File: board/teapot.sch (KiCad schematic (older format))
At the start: 48 parts, among them J1 MICROUSB, P1 BATT, P2 SMA, P3 SWD_TC, Q1 TEPT4400, U1 TPS79333DBVR, U2 TLV61225, U4 RFM69W, U5 STM32L052K6T6, U6 HTU21D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

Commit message: Sch: removed usb, pwr led, swd
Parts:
- removed C2: 100n, Capacitors_SMD:C_0603, symbol C
- removed C4: 10n, Capacitors_SMD:C_0603, symbol C
- removed C5: 10u, Capacitors_SMD:C_0603, symbol C
- removed D2: RED, LEDs:LED_0805, symbol LED
- removed J1: MICROUSB, agg:MICROUSB_MOLEX_47589-0001, symbol MICROUSB
- removed R2: 1k, Resistors_SMD:R_0603, symbol R
- removed U1: TPS79333DBVR, TO_SOT_Packages_SMD:SOT-23-5, symbol TPS79333DBVR
- removed U8: SWD, footprints:SWD, symbol SWD
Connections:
- net labels removed: +5V
- wire segments 91 -> 78
- no-connect marks 14 -> 10
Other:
- note removed: "10nF cap optional\nfor noise reduction"
- note removed: "USB"
- moved on the sheet: C1, C3, D1, D4, D5, L1, P1, R1, R5, R6, TP2, TP3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

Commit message: Migated PSU and boilerplate to new QFN-64 micro
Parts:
- removed U5: STM32L052K6T6, footprints:LQFP32_ST, symbol STM32L052K6T6
- added C?: 100n, Capacitors_SMD:C_0603, symbol C
- added IC?: STM32F0xxCxUx, agg:QFN-48-EP-ST, symbol STM32F0xxCxUx
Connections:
- net labels removed: USB_D+, USB_D-
- wire segments 78 -> 74
- no-connect marks 10 -> 5
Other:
- note added: "VBAT"
- note added: "VDD"
- note added: "VDDA"
- moved on the sheet: C10, C11, C12, C13, C15, C16, C8, C9, R3, R4, TP4, TP5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

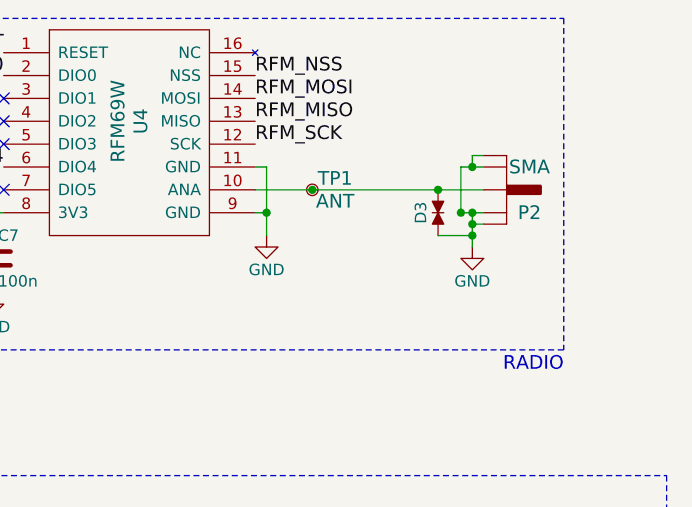
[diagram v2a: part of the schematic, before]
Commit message: Ripped up old PCB.
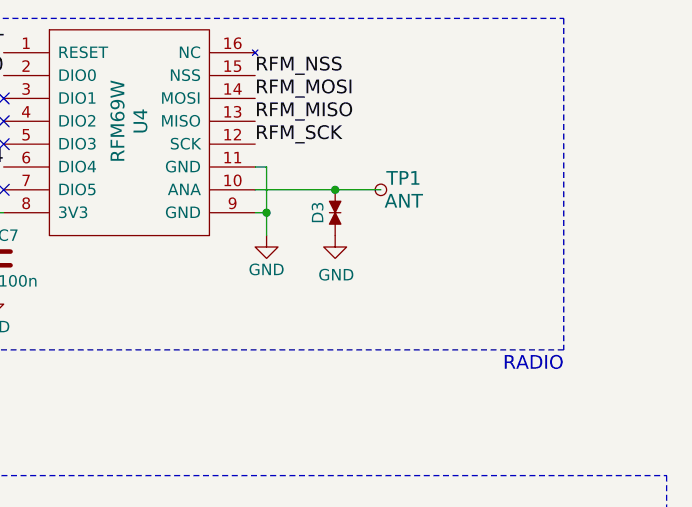
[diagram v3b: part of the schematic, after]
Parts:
- removed P2: SMA, footprints:SMA-142-0701-801, symbol SMA
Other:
- moved on the sheet: D3, TP1
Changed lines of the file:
@@
 RFM_SCK
-$Comp
-L SMA P2
-U 1 1 5670BE45
-P 10050 1650
-F 0 "P2" H 10150 1550 60  0000 C CNN
-F 1 "SMA" H 10150 1750 60  0000 C CNN
-F 2 "footprints:SMA-142-0701-801" H 10050 1650 60  0001 C CNN
-F 3 "" H 10050 1650 60  0000 C CNN
-F 4 "1342651" H 10050 1650 60  0001 C CNN "Farnell"
-	1    10050 1650
-	1    0    0    -1
-$EndComp
 $Comp
 L TestPoint TP1
 U 1 1 5670C17A
-P 9200 1650
-F 0 "TP1" H 9300 1700 60  0000 C CNN
-F 1 "ANT" H 9300 1600 60  0000 C CNN
-F 2 "footprints:Test_point" H 9200 1650 60  0001 C CNN
-F 3 "" H 9200 1650 60  0000 C CNN
-	1    9200 1650
-	1    0    0    -1
-$EndComp
-$Comp
-L GND #PWR014
-U 1 1 5670C5C3
-P 9900 1900
-F 0 "#PWR014" H 9900 1650 50  0001 C CNN
-F 1 "GND" H 9900 1750 50  0000 C CNN
-F 2 "" H 9900 1900 50  0000 C CNN
-F 3 "" H 9900 1900 50  0000 C CNN
-	1    9900 1900
+P 9500 1650
+F 0 "TP1" H 9600 1700 60  0000 C CNN
+F 1 "ANT" H 9600 1600 60  0000 C CNN
+F 2 "footprints:Test_point" H 9500 1650 60  0001 C CNN
+F 3 "" H 9500 1650 60  0000 C CNN
+	1    9500 1650
 	1    0    0    -1
 $EndComp
@@
 L TVS_small D3
 U 1 1 56787864
-P 9750 1750
-F 0 "D3" H 9750 1825 50  0000 C CNN
-F 1 "TVS_small" H 9750 1675 50  0001 C CNN
-F 2 "Resistors_SMD:R_0603" H 9750 1750 60  0001 C CNN
-F 3 "http://www.farnell.com/datasheets/1772768.pdf" H 9750 1750 60  0001 C CNN
-F 4 "2368174" H 9750 1750 60  0001 C CNN "Farnell"
-	1    9750 1750
+P 9300 1750
+F 0 "D3" H 9300 1825 50  0000 C CNN
+F 1 "TVS_small" H 9300 1675 50  0001 C CNN
+F 2 "Resistors_SMD:R_0603" H 9300 1750 60  0001 C CNN
+F 3 "http://www.farnell.com/datasheets/1772768.pdf" H 9300 1750 60  0001 C CNN
+F 4 "2368174" H 9300 1750 60  0001 C CNN "Farnell"
+	1    9300 1750
 	0    -1   -1   0
 $EndComp
@@
 Connection ~ 9850 4050
 Wire Wire Line
-	8950 1650 9950 1650
-Wire Wire Line
-	9850 1550 9950 1550
-Wire Wire Line
-	9900 1550 9900 1500
-Wire Wire Line
-	9900 1500 9950 1500
-Connection ~ 9900 1550
-Wire Wire Line
-	9900 1750 9900 1900
-Wire Wire Line
-	9900 1800 9950 1800
-Connection ~ 9900 1750
-Connection ~ 9200 1650
-Wire Wire Line
-	9850 1550 9850 1750
-Connection ~ 9850 1750
-Connection ~ 9900 1800
-Wire Wire Line
-	9850 1750 9950 1750
-Wire Wire Line
 	8950 1550 9000 1550
 Wire Wire Line
@@
 Wire Wire Line
 	7500 3250 7550 3250
-Connection ~ 9750 1650
+Connection ~ 9300 1650
 Wire Wire Line
 	1900 1050 1900 1500
@@
 Wire Wire Line
 	2200 1650 2200 1850
-Wire Wire Line
-	9750 1850 9900 1850
-Connection ~ 9900 1850
 Wire Wire Line
 	1900 1050 2050 1050
@@
 Text Notes -4050 2800 0    60   ~ 0
 VBAT
+$Comp
+L GND #PWR?
+U 1 1 5764CF24
+P 9300 1850
+F 0 "#PWR?" H 9300 1600 50  0001 C CNN
+F 1 "GND" H 9305 1677 50  0000 C CNN
+F 2 "" H 9300 1850 50  0000 C CNN
+F 3 "" H 9300 1850 50  0000 C CNN
+	1    9300 1850
+	1    0    0    -1
+$EndComp
+Wire Wire Line
+	8950 1650 9500 1650
 $EndSCHEMATC

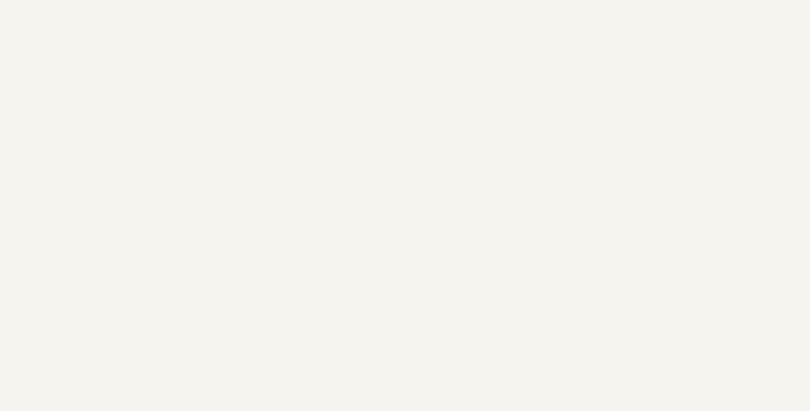
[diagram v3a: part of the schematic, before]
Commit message: Added AMG88 part/fp
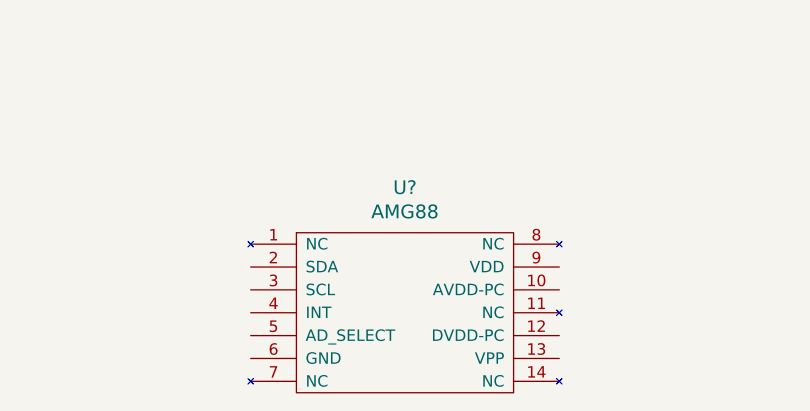
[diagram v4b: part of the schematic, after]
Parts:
- added U?: AMG88, footprints:AMG88, symbol AMG88
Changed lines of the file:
@@
 LIBS:tept
 LIBS:rfm69w
-LIBS:sma
 LIBS:testpoint
-LIBS:swd
-LIBS:tps79333dbvr
 LIBS:tvs_small
 LIBS:microusb
 LIBS:swd_tc
 LIBS:stm32f0xxcxux
+LIBS:amg88
 LIBS:teapot-cache
 EELAYER 25 0
@@
 Wire Wire Line
 	8950 1650 9500 1650
+$Comp
+L AMG88 U?
+U 1 1 57642B50
+P -3100 7400
+F 0 "U?" H -3125 7947 60  0000 C CNN
+F 1 "AMG88" H -3125 7841 60  0000 C CNN
+F 2 "footprints:AMG88" H -3150 7800 60  0001 C CNN
+F 3 "http://www.farnell.com/datasheets/1995912.pdf" H -3150 7800 60  0001 C CNN
+F 4 "2481446" H -3100 7400 60  0001 C CNN "Farnell"
+	1    -3100 7400
+	1    0    0    -1
+$EndComp
 $EndSCHEMATC

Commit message: Initial placement
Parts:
- added X101, X102, X103, X104: PART, Mounting_Holes:MountingHole_2.7mm_M2.5, symbol PART
- gave numbers to parts that had none: 3
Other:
- note added: "M2.5 Mounting Holes"

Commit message: Second placement
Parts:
- added C102: 1u, Capacitors_SMD:C_0603, symbol C
- added C103: 1.5uF, Capacitors_SMD:C_0603, symbol C
- added C104: 10u, Capacitors_SMD:C_0603, symbol C
- added R101: 20R, Resistors_SMD:R_0603, symbol R
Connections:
- net +3V3: now also U101.13 (VPP), U101.9 (VDD), C104.1
- net GND: now also U101.5 (AD_SELECT), U101.6 (GND), C103.2, C104.2, R101.2
- net I2C_SCK: now also U101.3 (SCL)
- net I2C_SDA: now also U101.2 (SDA)
- net at U101.10 (AVDD-PC): now also C102.1
- net at U101.12 (DVDD-PC): now also C103.1
- net AMG88_INT: now reaches U101.4 (INT)
- new net: C102.2, R101.1

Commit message: Pin assignment and final placement??
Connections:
- net AMG88_INT: now also IC101.45 (PB8)
- net BATT_MON: now also IC101.10 (PA0)
- net I2C_SCK: now also IC101.42 (PB6)
- net I2C_SDA: now also IC101.43 (PB7)
- net LED_GREEN: now also IC101.19 (PB1)
- net LED_YELLOW: now also IC101.18 (PB0)
- net LIGHT_EN: now also IC101.12 (PA2)
- net LIGHT_SENSE: now also IC101.13 (PA3)
- net RFM_MISO: now also IC101.40 (PB4)
- net RFM_MOSI: now also IC101.41 (PB5)
- net RFM_NSS: now also IC101.33 (PA12)
- net RFM_RESET: now also IC101.32 (PA11)
- net RFM_SCK: now also IC101.39 (PB3)
- net RFM_DIO0: no longer names the net of U4.2 (DIO0)
- net RFM_DIO4: no longer names the net of U4.6 (DIO4)
- no-connect marks 5 -> 7
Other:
- moved on the sheet: R3, R4, TP4, TP5
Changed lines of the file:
@@
 L R R4
 U 1 1 56708874
-P 5450 4050
-F 0 "R4" V 5550 4050 50  0000 C CNN
-F 1 "10k" V 5450 4050 50  0000 C CNN
-F 2 "Resistors_SMD:R_0603" V 5380 4050 50  0001 C CNN
-F 3 "" H 5450 4050 50  0000 C CNN
-F 4 "2447230" H 5450 4050 60  0001 C CNN "Farnell"
-	1    5450 4050
+P -1100 4550
+F 0 "R4" V -1000 4550 50  0000 C CNN
+F 1 "10k" V -1100 4550 50  0000 C CNN
+F 2 "Resistors_SMD:R_0603" V -1170 4550 50  0001 C CNN
+F 3 "" H -1100 4550 50  0000 C CNN
+F 4 "2447230" H -1100 4550 60  0001 C CNN "Farnell"
+	1    -1100 4550
 	1    0    0    -1
 $EndComp
@@
 L R R3
 U 1 1 567088B5
-P 5350 4050
-F 0 "R3" V 5250 4050 50  0000 C CNN
-F 1 "10k" V 5350 4050 50  0000 C CNN
-F 2 "Resistors_SMD:R_0603" V 5280 4050 50  0001 C CNN
-F 3 "" H 5350 4050 50  0000 C CNN
-F 4 "2447230" H 5350 4050 60  0001 C CNN "Farnell"
-	1    5350 4050
+P -1200 4550
+F 0 "R3" V -1300 4550 50  0000 C CNN
+F 1 "10k" V -1200 4550 50  0000 C CNN
+F 2 "Resistors_SMD:R_0603" V -1270 4550 50  0001 C CNN
+F 3 "" H -1200 4550 50  0000 C CNN
+F 4 "2447230" H -1200 4550 60  0001 C CNN "Farnell"
+	1    -1200 4550
 	1    0    0    1
 $EndComp
@@
 L +3V3 #PWR010
 U 1 1 56708996
-P 5400 3850
-F 0 "#PWR010" H 5400 3700 50  0001 C CNN
-F 1 "+3V3" H 5400 3990 50  0000 C CNN
-F 2 "" H 5400 3850 50  0000 C CNN
-F 3 "" H 5400 3850 50  0000 C CNN
-	1    5400 3850
+P -1150 4350
+F 0 "#PWR010" H -1150 4200 50  0001 C CNN
+F 1 "+3V3" H -1150 4490 50  0000 C CNN
+F 2 "" H -1150 4350 50  0000 C CNN
+F 3 "" H -1150 4350 50  0000 C CNN
+	1    -1150 4350
 	1    0    0    -1
 $EndComp
@@
 Text Notes 10300 2450 2    60   ~ 0
 RADIO
-Text Label 4650 4400 0    60   ~ 0
+Text Label -2100 4900 0    60   ~ 0
 I2C_SCK
-Text Label 1650 5150 2    60   ~ 0
+Text Label -2100 2800 0    60   ~ 0
 LIGHT_SENSE
-Text Label 4650 3500 0    60   ~ 0
+Text Label -2100 3700 0    60   ~ 0
 RFM_RESET
-Text Label 4650 4000 0    60   ~ 0
+Text Label -2100 3800 0    60   ~ 0
 RFM_NSS
-Text Label 4650 4100 0    60   ~ 0
+Text Label -2100 4600 0    60   ~ 0
 RFM_SCK
-Text Label 4650 4200 0    60   ~ 0
+Text Label -2100 4700 0    60   ~ 0
 RFM_MISO
-Text Label 4650 4300 0    60   ~ 0
+Text Label -2100 4800 0    60   ~ 0
 RFM_MOSI
-Text Label 1650 4850 2    60   ~ 0
+Text Label -2100 4300 0    60   ~ 0
 LED_YELLOW
-Text Label 1650 4950 2    60   ~ 0
+Text Label -2100 4400 0    60   ~ 0
 LED_GREEN
 Text Label 9500 5150 2    60   ~ 0
@@
 	0    -1   -1   0
 $EndComp
-Text Label 1650 5250 2    60   ~ 0
+Text Label -2100 2700 0    60   ~ 0
 LIGHT_EN
 Text Label 9850 3350 2    60   ~ 0
@@
 Text Label 2350 1050 0    60   ~ 0
 BATT_MON
-Text Label 1650 5050 2    60   ~ 0
+Text Label -2100 2500 0    60   ~ 0
 BATT_MON
 Text Notes 10050 6300 2    60   ~ 0
@@
 L TestPoint TP4
 U 1 1 5684D483
-P 5350 4250
-F 0 "TP4" H 5225 4225 60  0000 C CNN
-F 1 "SCK" H 5250 4300 60  0000 C CNN
-F 2 "footprints:Test_point_mini" H 5350 4250 60  0001 C CNN
-F 3 "" H 5350 4250 60  0000 C CNN
-	1    5350 4250
+P -1200 4750
+F 0 "TP4" H -1325 4725 60  0000 C CNN
+F 1 "SCK" H -1300 4800 60  0000 C CNN
+F 2 "footprints:Test_point_mini" H -1200 4750 60  0001 C CNN
+F 3 "" H -1200 4750 60  0000 C CNN
+	1    -1200 4750
 	1    0    0    -1
 $EndComp
@@
 L TestPoint TP5
 U 1 1 5684D727
-P 5450 4250
-F 0 "TP5" H 5550 4225 60  0000 C CNN
-F 1 "SDA" H 5550 4300 60  0000 C CNN
-F 2 "footprints:Test_point_mini" H 5450 4250 60  0001 C CNN
-F 3 "" H 5450 4250 60  0000 C CNN
-	1    5450 4250
+P -1100 4750
+F 0 "TP5" H -1000 4725 60  0000 C CNN
+F 1 "SDA" H -1000 4800 60  0000 C CNN
+F 2 "footprints:Test_point_mini" H -1100 4750 60  0001 C CNN
+F 3 "" H -1100 4750 60  0000 C CNN
+	1    -1100 4750
 	1    0    0    -1
 $EndComp
@@
 	1    0    0    -1
 $EndComp
-Text Label 7850 1550 2    60   ~ 0
-RFM_DIO4
-Text Label 7850 1150 2    60   ~ 0
-RFM_DIO0
-Text Label 4650 3300 0    60   ~ 0
-RFM_DIO0
-Text Label 4650 3400 0    60   ~ 0
-RFM_DIO4
 $Comp
 L STM32F0xxCxUx IC101
@@
 Text Notes -5050 2800 0    60   ~ 0
 VDD
-Text Label 4650 4500 0    60   ~ 0
+Text Label -2100 5000 0    60   ~ 0
 I2C_SDA
 $Comp
@@
 	9900 5150 9900 5300
 Wire Wire Line
-	5400 3850 5400 3900
-Wire Wire Line
-	5350 3900 5450 3900
-Connection ~ 5400 3900
+	-1150 4350 -1150 4400
+Wire Wire Line
+	-1200 4400 -1100 4400
+Connection ~ -1150 4400
 Connection ~ 7300 3450
 Wire Wire Line
@@
 	7300 2350 7300 900
 Connection ~ 4200 1450
-Connection ~ 5450 4250
-Connection ~ 5350 4250
+Connection ~ -1100 4750
+Connection ~ -1200 4750
 Wire Wire Line
 	3500 5325 3550 5325
@@
 Connection ~ -4950 2200
 Wire Wire Line
-	5350 4200 5350 4400
-Wire Wire Line
-	5350 4400 4650 4400
-Wire Wire Line
-	5450 4200 5450 4500
-Wire Wire Line
-	5450 4500 4650 4500
+	-1200 4900 -1200 4700
+Wire Wire Line
+	-2100 4900 -1200 4900
+Wire Wire Line
+	-1100 5000 -1100 4700
+Wire Wire Line
+	-2100 5000 -1100 5000
 Connection ~ -3600 3900
 Connection ~ -3600 4100
@@
 Wire Wire Line
 	-1600 7300 -1600 7450
+NoConn ~ 7850 1150
+NoConn ~ 7850 1550
+Text Label -2100 5200 0    60   ~ 0
+AMG88_INT
 $EndSCHEMATC

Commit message: First route
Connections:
- net AMG88_INT: now also IC101.2 (PC13); no longer IC101.45 (PB8)
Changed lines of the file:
@@
 NoConn ~ 7850 1150
 NoConn ~ 7850 1550
-Text Label -2100 5200 0    60   ~ 0
+Text Label -2900 3800 2    60   ~ 0
 AMG88_INT
 $EndSCHEMATC
